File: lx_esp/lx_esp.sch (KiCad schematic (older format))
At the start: 15 parts

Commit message: programming header for esp module
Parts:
- removed R? (x2): R, symbol R
- removed SW? (x2): SW_Push, symbol SW_Push
- added C? (x2): C, symbol C
- added J?: Conn_02x05_Odd_Even, symbol Conn_02x05_Odd_Even
- added J?: Conn_01x02, symbol Conn_01x02
- added R? (x5): R, symbol R
- added U?: MCP1700-3302E_SOT89, TO_SOT_Packages_SMD:SOT89-3_Housing, symbol MCP1700-3302E_SOT89
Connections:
- net labels added: +BATT
- wire segments 118 -> 132
- no-connect marks 10 -> 9
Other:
- note added: "PROG"
- note added: "Vmon"
- note removed: "Boot"
- note removed: "Flash"
- moved on the sheet: C?, J?, R?, SW?, U?

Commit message: LTC4365
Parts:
- removed J?: Conn_02x05_Odd_Even, symbol Conn_02x05_Odd_Even
- added C?: 680u, symbol CP1
- added Q? (x2): Dual_Nch_MOSFET, symbol Dual_Nch_MOSFET
- added R? (x3): 249k, symbol R
- added R?: 2.49M, symbol R
- added R?: R, symbol R
- added SW?: SW_Push, symbol SW_Push
- added U?: LTC4365, symbol LTC4365
- R? (x2): value R -> 249k
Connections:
- wire segments 132 -> 176
- no-connect marks 9 -> 11
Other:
- moved on the sheet: J?, R?

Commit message: new power supply
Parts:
- removed U?: MCP1700-3302E_SOT89, TO_SOT_Packages_SMD:SOT89-3_Housing, symbol MCP1700-3302E_SOT89
- added R?: R, symbol R
- added U?: XC6210, symbol XC6210
- C? (x3): value C -> 1u
- C?: value C -> 10u
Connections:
- net GND: now also U?.2 (Vss)
- net +3V3 renamed VCC
- net VCC: now also U?.5 (Vout)
- net +BATT: no longer names the net of C?.1, Q?.1 (D), R?.1, U?.7 (Vout)
- net +BATT: now also R?.2, U?.4 (Vin)
- new net: R?.1, U?.1 (CE)
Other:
- moved on the sheet: C?, R?

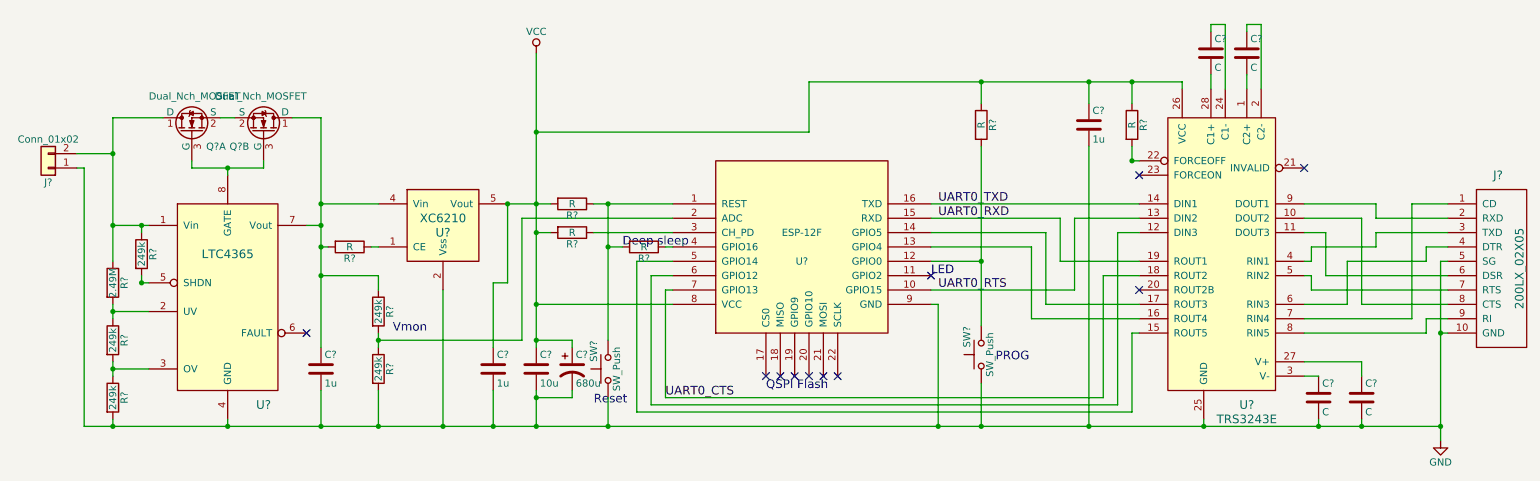
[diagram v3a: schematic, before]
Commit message: Swap TRS3243 to TRS3238
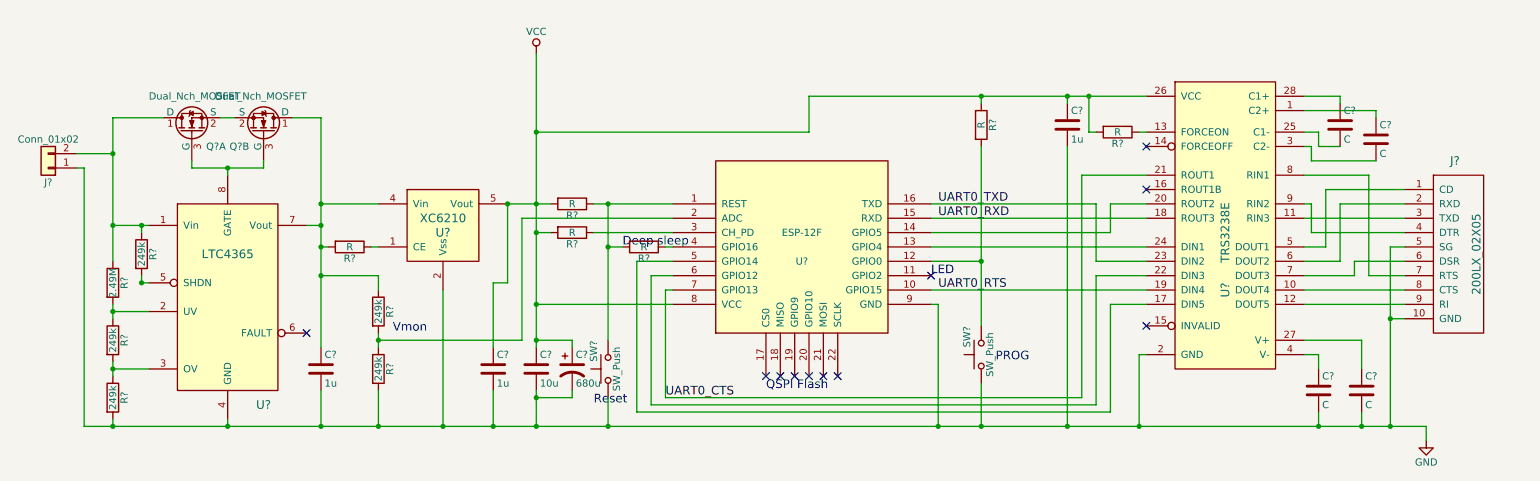
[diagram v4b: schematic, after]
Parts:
- removed U?: TRS3243E, symbol TRS3243E
- added U?: TRS3238E, symbol TRS3238E
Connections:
- net GND: now also U?.2 (GND)
- net UART0_CTS: now also U?.21 (ROUT1)
- net UART0_RTS: now also U?.19 (DIN4)
- net UART0_RXD: now also U?.18 (ROUT3)
- net UART0_TXD: now also U?.23 (DIN2)
- net VCC: now also R?.2, U?.26 (VCC); no longer R?.1
- net at C?.2: now also U?.3 (C2-)
- net at J?.8 (CTS): now also U?.10 (DOUT4)
- net at J?.6 (DSR): now also U?.7 (DOUT3)
- net at U?.6 (GPIO12): now also U?.22 (DIN3)
- net at U?.5 (GPIO14): now also U?.17 (DIN5)
- net at U?.13 (GPIO4): now also U?.24 (DIN1)
- net at U?.14 (GPIO5): now also U?.20 (ROUT2)
- net at C?.1: now also U?.1 (C2+)
- net at C?.1: now also U?.28 (C1+)
- net at C?.1: now also U?.27 (V+)
- net at C?.2: now also U?.25 (C1-)
- net at C?.1: now also U?.4 (V-)
- net at J?.3 (TXD): now also U?.11 (RIN3)
- net at J?.7 (RTS): now also U?.8 (RIN1)
- net at J?.4 (DTR): now also U?.9 (RIN2)
- net at J?.1 (CD): now also U?.5 (DOUT1)
- net at J?.9 (RI): now also U?.12 (DOUT5)
- net at J?.2 (RXD): now also U?.6 (DOUT2)
- new net: R?.1, U?.13 (FORCEON)
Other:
- moved on the sheet: C?, J?, R?

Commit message: assign footprints for chips
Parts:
- J?: footprint (none) -> ssop_20:CONN_02x05_2mm
- Q?: footprint (none) -> Housings_SOIC:SOIC-8_3.9x4.9mm_Pitch1.27mm
- U?: footprint (none) -> ESP8266:ESP-12E_SMD
- U?: footprint (none) -> TO_SOT_Packages_SMD:TSOT-23-8_HandSoldering
- U?: footprint (none) -> TO_SOT_Packages_SMD:SOT89-5_Housing_Handsoldering
- U?: footprint (none) -> ssop_20:(T)SSOP-28
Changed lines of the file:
@@
 F 0 "J?" H 10500 2750 60  0000 C CNN
 F 1 "200LX_02X05" V 10650 2100 60  0000 C CNN
-F 2 "" H 10300 2700 60  0001 C CNN
+F 2 "ssop_20:CONN_02x05_2mm" H 10300 2700 60  0001 C CNN
 F 3 "" H 10300 2700 60  0001 C CNN
 	1    10500 2850
@@
 F 0 "U?" H 5950 3450 50  0000 C CNN
 F 1 "ESP-12F" H 5950 3650 50  0000 C CNN
-F 2 "" H 5950 3550 50  0001 C CNN
+F 2 "ESP8266:ESP-12E_SMD" H 5950 3550 50  0001 C CNN
 F 3 "" H 5950 3550 50  0001 C CNN
 	1    5950 3550
@@
 F 0 "U?" H 2200 3150 60  0000 C CNN
 F 1 "LTC4365" H 1950 4200 60  0000 C CNN
-F 2 "" H 2050 3800 60  0001 C CNN
+F 2 "TO_SOT_Packages_SMD:TSOT-23-8_HandSoldering" H 2050 3800 60  0001 C CNN
 F 3 "" H 2050 3800 60  0001 C CNN
 	1    1950 3900
@@
 F 0 "Q?" H 1800 2750 50  0000 L CNN
 F 1 "Dual_Nch_MOSFET" H 1400 3100 50  0000 L CNN
-F 2 "" H 1500 3000 50  0001 C CNN
+F 2 "Housings_SOIC:SOIC-8_3.9x4.9mm_Pitch1.27mm" H 1500 3000 50  0001 C CNN
 F 3 "" V 1700 2850 50  0001 C CNN
 	1    1700 2800
@@
 F 0 "U?" H 3450 3350 60  0000 C CNN
 F 1 "XC6210" H 3450 3450 60  0000 C CNN
-F 2 "" H 3450 3400 60  0001 C CNN
+F 2 "TO_SOT_Packages_SMD:SOT89-5_Housing_Handsoldering" H 3450 3400 60  0001 C CNN
 F 3 "" H 3450 3400 60  0001 C CNN
 	1    3450 3400
@@
 F 0 "U?" V 8900 3050 60  0000 C CNN
 F 1 "TRS3238E" V 8900 3450 60  0000 C CNN
-F 2 "" H 8900 3450 60  0001 C CNN
+F 2 "ssop_20:(T)SSOP-28" H 8900 3450 60  0001 C CNN
 F 3 "" H 8900 3450 60  0001 C CNN
 	1    8900 3450

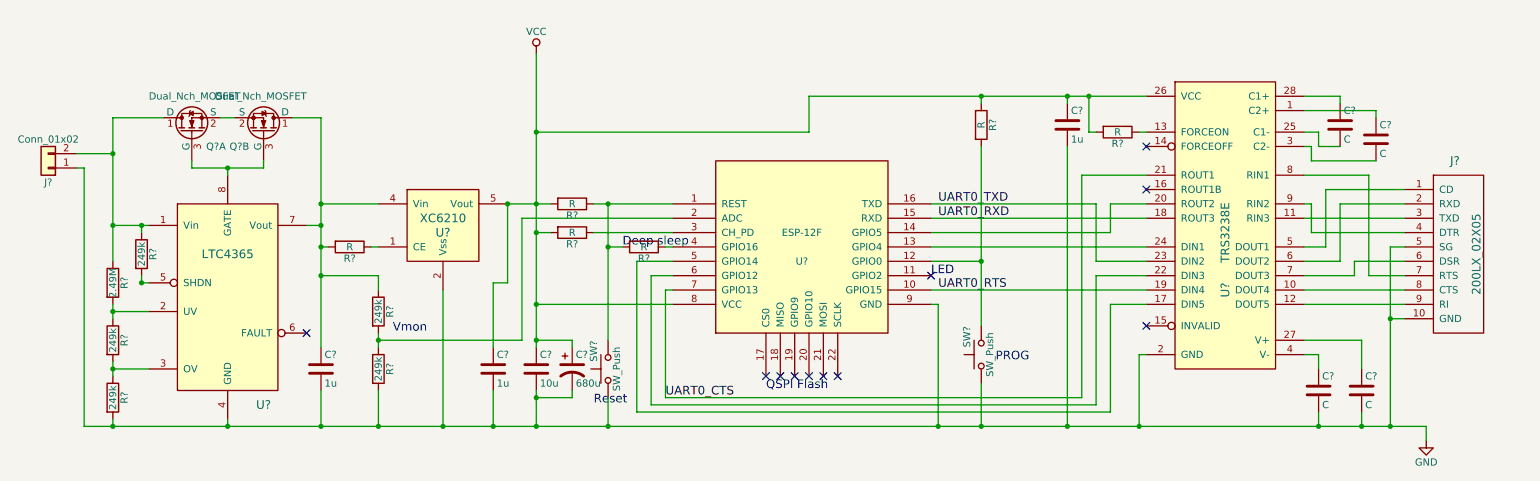
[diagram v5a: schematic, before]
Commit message: footprints and designators and stuff
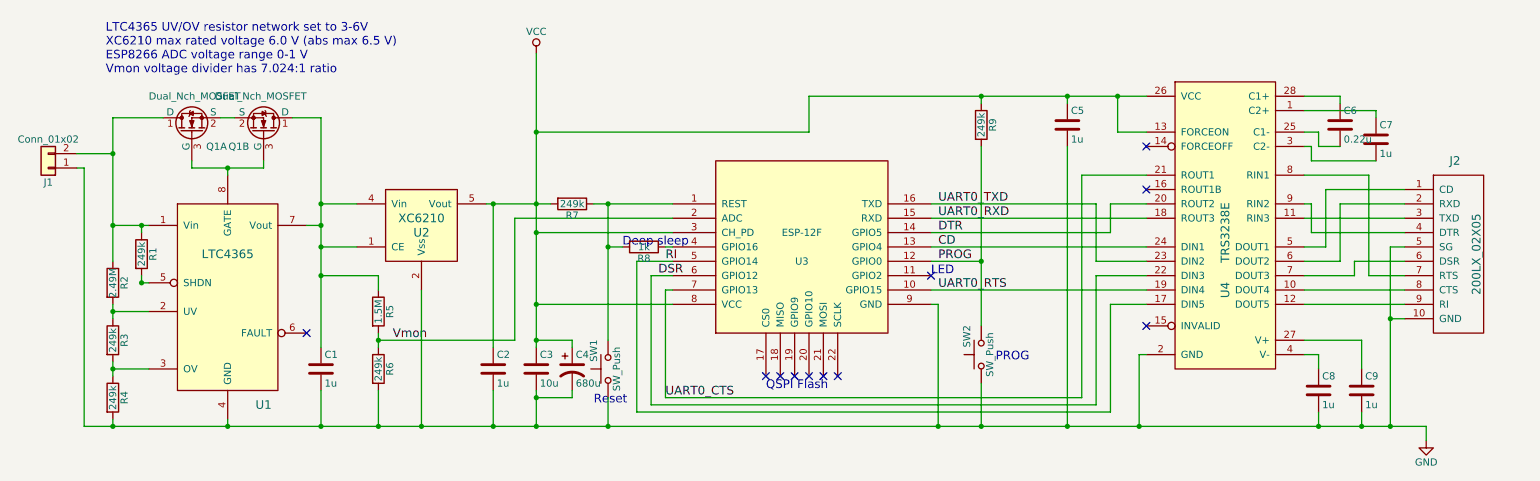
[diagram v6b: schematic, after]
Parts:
- removed R? (x3): R, symbol R
- C6: renamed from C?; value C -> 0.22u
- C7, C8, C9: renamed from C?; value C -> 1u
- R5: renamed from R?; value 249k -> 1.5M
- R7, R9: renamed from R?; value R -> 249k
- R8: renamed from R?; value R -> 1k
- gave numbers to parts that had none: 19
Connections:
- net VCC: now also U3.3 (CH_PD), U4.13 (FORCEON)
- net PROG: now reaches R9.2, SW2.2, U3.12 (GPIO0)
- net CD: now reaches U3.13 (GPIO4), U4.24 (DIN1)
- net DTR: now reaches U3.14 (GPIO5), U4.20 (ROUT2)
- net Vmon: now reaches R5.2, R6.1, U3.2 (ADC)
- net RI: now reaches U3.5 (GPIO14), U4.17 (DIN5)
- net DSR: now reaches U3.6 (GPIO12), U4.22 (DIN3)
- net at C1.1, Q1.1 (D), R5.1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: now also U2.1 (CE)
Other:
- note added: "LTC4365 UV/OV resistor network set to 3-6V\nXC6210 max rated voltage 6.0 V (abs max 6.5 V)\nESP8266 ADC voltage range 0-1 V\nVmon voltage divider has 7.024:1 ratio"
- note removed: "Vmon"
- moved on the sheet: U2

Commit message: footprints for passives
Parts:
- C1, C2, C3, C5, C6, C7, C8, C9: footprint (none) -> Capacitors_SMD:C_0805_HandSoldering
- C4: footprint (none) -> Capacitors_THT:CP_Radial_D10.0mm_P5.00mm
- J1: footprint (none) -> Pin_Headers:Pin_Header_Straight_1x02_Pitch2.54mm
- Q1: footprint (none) -> Housings_SOIC:SOIC-8_3.9x4.9mm_Pitch1.27mm
- R1, R2, R3, R4, R5, R6, R7, R8, R9: footprint (none) -> Resistors_SMD:R_0805_HandSoldering
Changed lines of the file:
@@
 F 0 "C8" H 9575 4650 50  0000 L CNN
 F 1 "1u" H 9575 4450 50  0000 L CNN
-F 2 "" H 9588 4400 50  0001 C CNN
+F 2 "Capacitors_SMD:C_0805_HandSoldering" H 9588 4400 50  0001 C CNN
 F 3 "" H 9550 4550 50  0001 C CNN
 	1    9550 4550
@@
 F 0 "C9" H 9875 4650 50  0000 L CNN
 F 1 "1u" H 9875 4450 50  0000 L CNN
-F 2 "" H 9888 4400 50  0001 C CNN
+F 2 "Capacitors_SMD:C_0805_HandSoldering" H 9888 4400 50  0001 C CNN
 F 3 "" H 9850 4550 50  0001 C CNN
 	1    9850 4550
@@
 F 0 "C6" H 9725 2800 50  0000 L CNN
 F 1 "0.22u" H 9725 2600 50  0000 L CNN
-F 2 "" H 9738 2550 50  0001 C CNN
+F 2 "Capacitors_SMD:C_0805_HandSoldering" H 9738 2550 50  0001 C CNN
 F 3 "" H 9700 2700 50  0001 C CNN
 	1    9700 2700
@@
 F 0 "C7" H 9975 2900 50  0000 L CNN
 F 1 "1u" H 9975 2700 50  0000 L CNN
-F 2 "" H 9988 2650 50  0001 C CNN
+F 2 "Capacitors_SMD:C_0805_HandSoldering" H 9988 2650 50  0001 C CNN
 F 3 "" H 9950 2800 50  0001 C CNN
 	1    9950 2800
@@
 F 0 "C5" H 7825 2800 50  0000 L CNN
 F 1 "1u" H 7825 2600 50  0000 L CNN
-F 2 "" H 7838 2550 50  0001 C CNN
+F 2 "Capacitors_SMD:C_0805_HandSoldering" H 7838 2550 50  0001 C CNN
 F 3 "" H 7800 2700 50  0001 C CNN
 	1    7800 2700
@@
 F 0 "C3" H 4125 4500 50  0000 L CNN
 F 1 "10u" H 4125 4300 50  0000 L CNN
-F 2 "" H 4138 4250 50  0001 C CNN
+F 2 "Capacitors_SMD:C_0805_HandSoldering" H 4138 4250 50  0001 C CNN
 F 3 "" H 4100 4400 50  0001 C CNN
 	1    4100 4400
@@
 F 0 "R8" V 4930 3550 50  0000 C CNN
 F 1 "1k" V 4850 3550 50  0000 C CNN
-F 2 "" V 4780 3550 50  0001 C CNN
+F 2 "Resistors_SMD:R_0805_HandSoldering" V 4780 3550 50  0001 C CNN
 F 3 "" H 4850 3550 50  0001 C CNN
 	1    4850 3550
@@
 F 0 "R7" V 4430 3250 50  0000 C CNN
 F 1 "249k" V 4350 3250 50  0000 C CNN
-F 2 "" V 4280 3250 50  0001 C CNN
+F 2 "Resistors_SMD:R_0805_HandSoldering" V 4280 3250 50  0001 C CNN
 F 3 "" H 4350 3250 50  0001 C CNN
 	1    4350 3250
@@
 F 0 "C2" H 3825 4500 50  0000 L CNN
 F 1 "1u" H 3825 4300 50  0000 L CNN
-F 2 "" H 3838 4250 50  0001 C CNN
+F 2 "Capacitors_SMD:C_0805_HandSoldering" H 3838 4250 50  0001 C CNN
 F 3 "" H 3800 4400 50  0001 C CNN
 	1    3800 4400
@@
 F 0 "C1" H 2625 4500 50  0000 L CNN
 F 1 "1u" H 2625 4300 50  0000 L CNN
-F 2 "" H 2638 4250 50  0001 C CNN
+F 2 "Capacitors_SMD:C_0805_HandSoldering" H 2638 4250 50  0001 C CNN
 F 3 "" H 2600 4400 50  0001 C CNN
 	1    2600 4400
@@
 F 0 "J1" H 700 3100 50  0000 C CNN
 F 1 "Conn_01x02" H 700 2800 50  0000 C CNN
-F 2 "" H 700 3000 50  0001 C CNN
+F 2 "Pin_Headers:Pin_Header_Straight_1x02_Pitch2.54mm" H 700 3000 50  0001 C CNN
 F 3 "" H 700 3000 50  0001 C CNN
 	1    700  3000
@@
 F 0 "R5" V 3080 4000 50  0000 C CNN
 F 1 "1.5M" V 3000 4000 50  0000 C CNN
-F 2 "" V 2930 4000 50  0001 C CNN
+F 2 "Resistors_SMD:R_0805_HandSoldering" V 2930 4000 50  0001 C CNN
 F 3 "" H 3000 4000 50  0001 C CNN
 	1    3000 4000
@@
 F 0 "R6" V 3080 4400 50  0000 C CNN
 F 1 "249k" V 3000 4400 50  0000 C CNN
-F 2 "" V 2930 4400 50  0001 C CNN
+F 2 "Resistors_SMD:R_0805_HandSoldering" V 2930 4400 50  0001 C CNN
 F 3 "" H 3000 4400 50  0001 C CNN
 	1    3000 4400
@@
 F 0 "R3" V 1230 4200 50  0000 C CNN
 F 1 "249k" V 1150 4200 50  0000 C CNN
-F 2 "" V 1080 4200 50  0001 C CNN
+F 2 "Resistors_SMD:R_0805_HandSoldering" V 1080 4200 50  0001 C CNN
 F 3 "" H 1150 4200 50  0001 C CNN
 	1    1150 4200
@@
 F 0 "R4" V 1230 4600 50  0000 C CNN
 F 1 "249k" V 1150 4600 50  0000 C CNN
-F 2 "" V 1080 4600 50  0001 C CNN
+F 2 "Resistors_SMD:R_0805_HandSoldering" V 1080 4600 50  0001 C CNN
 F 3 "" H 1150 4600 50  0001 C CNN
 	1    1150 4600
@@
 F 0 "R1" V 1430 3600 50  0000 C CNN
 F 1 "249k" V 1350 3600 50  0000 C CNN
-F 2 "" V 1280 3600 50  0001 C CNN
+F 2 "Resistors_SMD:R_0805_HandSoldering" V 1280 3600 50  0001 C CNN
 F 3 "" H 1350 3600 50  0001 C CNN
 	1    1350 3600
@@
 F 0 "R2" V 1230 3800 50  0000 C CNN
 F 1 "2.49M" V 1150 3800 50  0000 C CNN
-F 2 "" V 1080 3800 50  0001 C CNN
+F 2 "Resistors_SMD:R_0805_HandSoldering" V 1080 3800 50  0001 C CNN
 F 3 "" H 1150 3800 50  0001 C CNN
 	1    1150 3800
@@
 F 0 "Q1" H 2300 2750 50  0000 L CNN
 F 1 "Dual_Nch_MOSFET" H 1900 3100 50  0000 L CNN
-F 2 "" H 2000 3000 50  0001 C CNN
+F 2 "Housings_SOIC:SOIC-8_3.9x4.9mm_Pitch1.27mm" H 2000 3000 50  0001 C CNN
 F 3 "" V 2200 2850 50  0001 C CNN
 	2    2200 2800
@@
 F 0 "C4" H 4375 4500 50  0000 L CNN
 F 1 "680u" H 4375 4300 50  0000 L CNN
-F 2 "" H 4350 4400 50  0001 C CNN
+F 2 "Capacitors_THT:CP_Radial_D10.0mm_P5.00mm" H 4350 4400 50  0001 C CNN
 F 3 "" H 4350 4400 50  0001 C CNN
 	1    4350 4400
@@
 F 0 "R9" V 7280 2700 50  0000 C CNN
 F 1 "249k" V 7200 2700 50  0000 C CNN
-F 2 "" V 7130 2700 50  0001 C CNN
+F 2 "Resistors_SMD:R_0805_HandSoldering" V 7130 2700 50  0001 C CNN
 F 3 "" H 7200 2700 50  0001 C CNN
 	1    7200 2700
@@
 	6850 3950 6900 3950
 Wire Wire Line
-	6900 4800 6900 3950
+	6900 3950 6900 4800
 Wire Wire Line
 	5050 3850 5000 3850
@@
 	3000 3850 3000 3750
 Wire Wire Line
-	2600 3750 3000 3750
+	3000 3750 2600 3750
 Connection ~ 2600 3750
 Wire Wire Line
